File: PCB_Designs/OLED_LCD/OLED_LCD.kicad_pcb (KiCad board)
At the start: 2 copper layers, 110 x 69.5 mm, 27 parts, among them P1 CONN_01X10, P2 CONN_01X16, P3 CONN_01X01, P4 CONN_01X01, P5 CONN_01X01, P6 CONN_01X01, SW1 Rotary_Encoder_Switch, U2 MCP23017, U3 CHERRY-MX

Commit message: Manufacture files added
* Gerbers created
* Drillfiles created
* G-CODE generated (milling information)
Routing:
- net /VCC5: track 404.0 -> 405.6 mm
- net GND: vias 12 -> 13
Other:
- board size 110 x 69.5 mm -> 110 x 60 mm

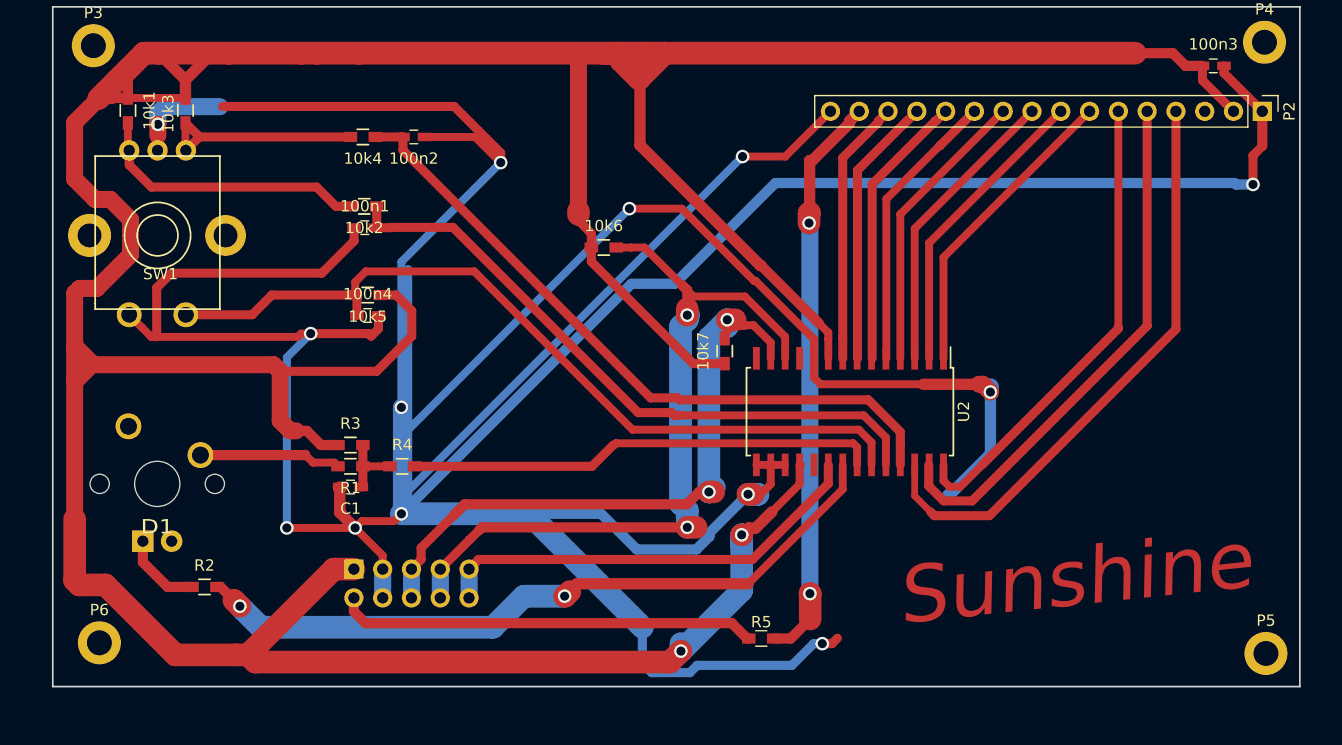
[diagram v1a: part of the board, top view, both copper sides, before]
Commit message: Hotfixes, updates and Photomask
* Edited small error in component placing (OLED_LCD)
* Updated all photomasks in light of recent events
* Generated photomask for OLED_LCD (.pdf)
* Updated all Gerberfiles (.gbr)
* Updated all drillfiles, now merging "plated" and unplated TH (.drl)
* With merge; all Non Plated Through Hole drills deleted (-NPTH.drl)
* Generated new G-CODE for all PCB (.ngc, .svg)
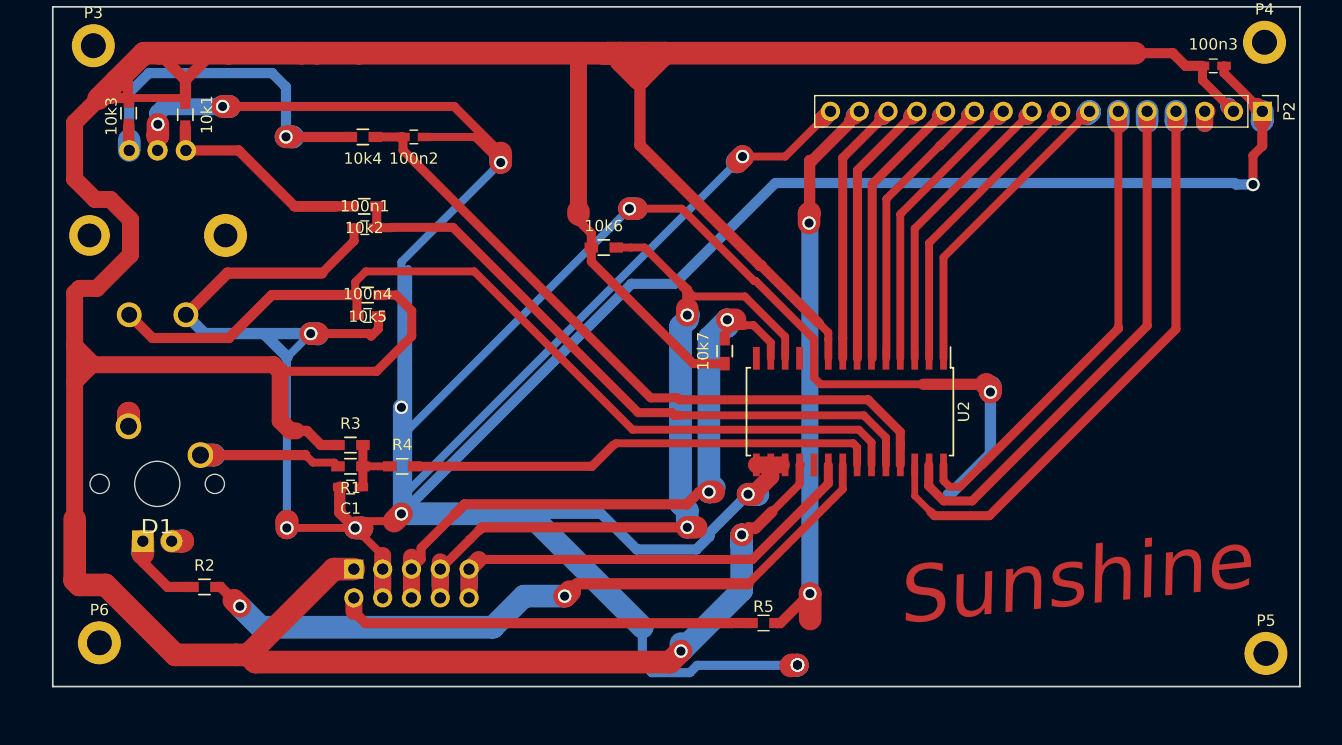
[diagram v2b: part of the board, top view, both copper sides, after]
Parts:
- SW1: moved to B.Cu
- moved 10k1 5.08 mm to (90.1, 87.8)
- moved 10k3 5.02 mm to (85.1, 87.7)
- moved R5 1.38 mm to (141.1, 132.7)
- turned SW1 to 0 degrees
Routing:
- net Net-(10k3-Pad1): track 19.2 -> 34.4 mm, vias 0 -> 1
- net /ENCODERSW: track 72.9 -> 82.0 mm
- net GND: track 519.4 -> 527.8 mm, vias 13 -> 15
- net /SDA#: track 58.5 -> 61.2 mm
- net Net-(10k1-Pad2): track 24.9 -> 22.4 mm
- net Net-(P2-Pad3): track 0.36 -> 2.71 mm
- net Net-(R1-Pad2): track 12.6 -> 14.9 mm
- net /SCL#: track 69.5 -> 71.7 mm
- net Net-(D1-Pad2): track 7.10 -> 9.21 mm
- net /INTA: track 39.1 -> 40.7 mm
- net /LCD_BACKLIGHT: track 50.7 -> 52.1 mm
- net /E: track 42.0 -> 43.3 mm
- net /D7: track 23.5 -> 24.7 mm
- net /D6: track 24.0 -> 25.2 mm
- net /D5: track 24.5 -> 25.7 mm
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
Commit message: New stuff
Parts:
- moved 100n2 5.25 mm to (106.0, 92.9), turned to 0 degrees
- moved 10k3 4.99 mm to (90.1, 87.7)
- moved 10k1 4.98 mm to (85.1, 87.6)
- moved 10k4 1.23 mm to (106.0, 91.0)
- moved 10k2 1.08 mm to (106.0, 94.9)
- moved 100n1 1.08 mm to (106.1, 96.7)
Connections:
- SW1 pad 1: Net-(10k3-Pad1) -> Net-(10k1-Pad2)
- SW1 pad 3: Net-(10k1-Pad2) -> Net-(10k3-Pad1)
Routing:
- net Net-(10k3-Pad1): track 34.4 -> 26.0 mm, vias 1 -> 0
- net GND: track 527.8 -> 521.3 mm
- net Net-(10k1-Pad2): track 22.4 -> 24.5 mm
- net /ENCODERB: track 57.2 -> 57.7 mm

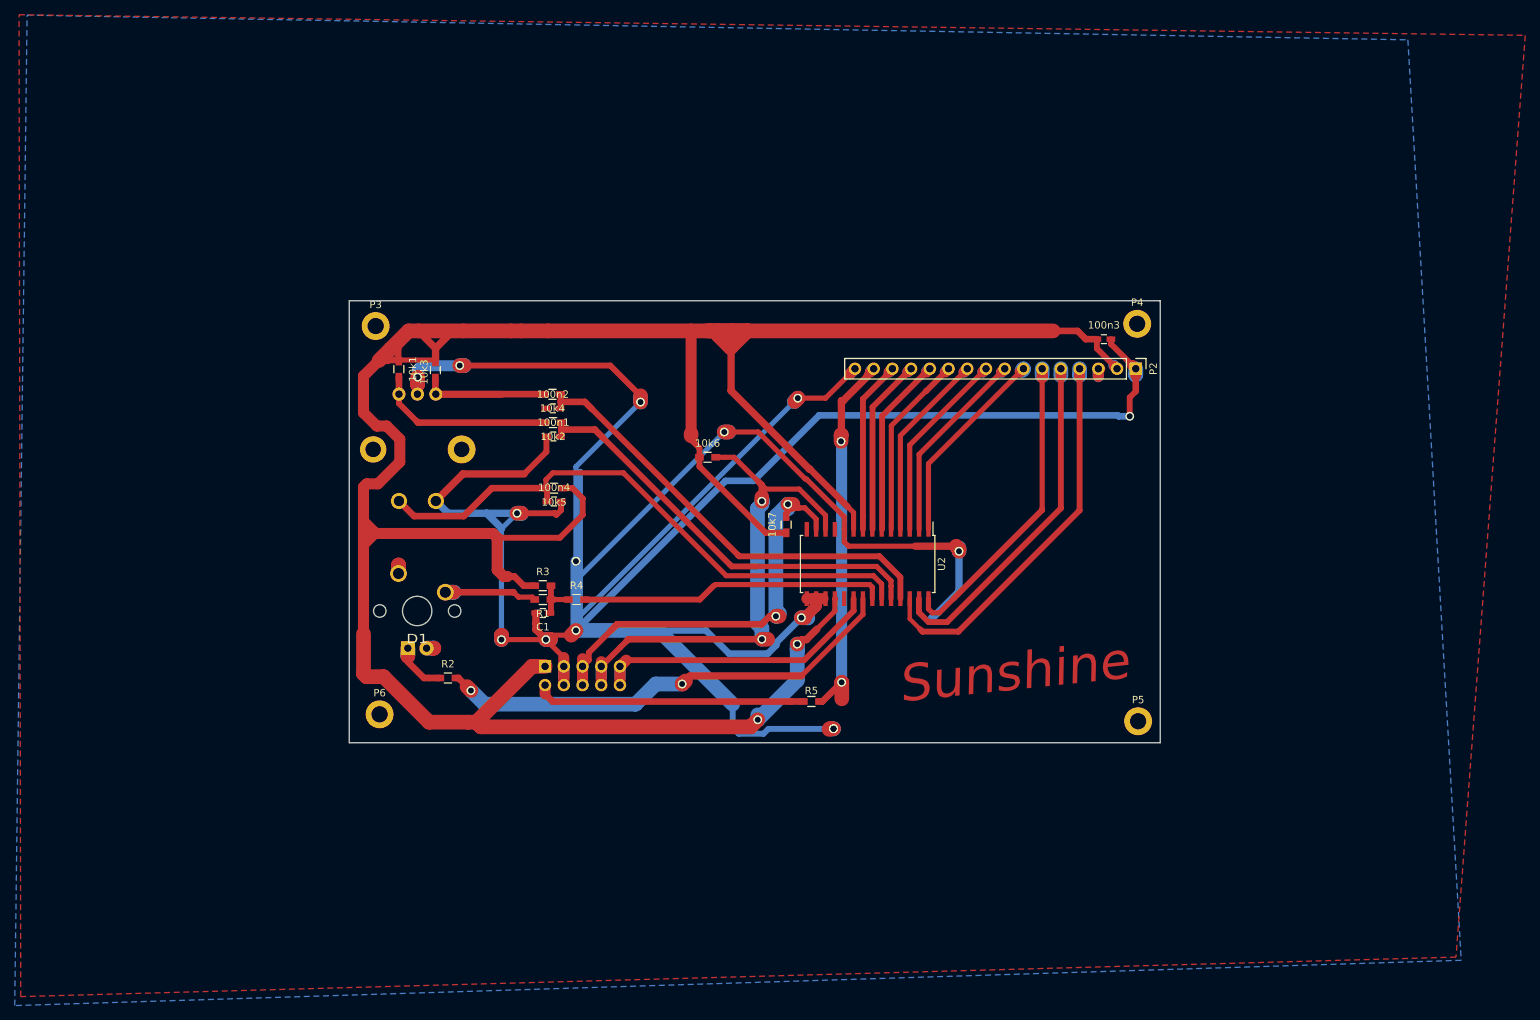
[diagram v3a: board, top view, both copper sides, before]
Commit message: OLED new layout
* Added few components to OLED_LCD pcb.
* Extended PCB layout to make room for all components.
* Generated new LCD photomasks
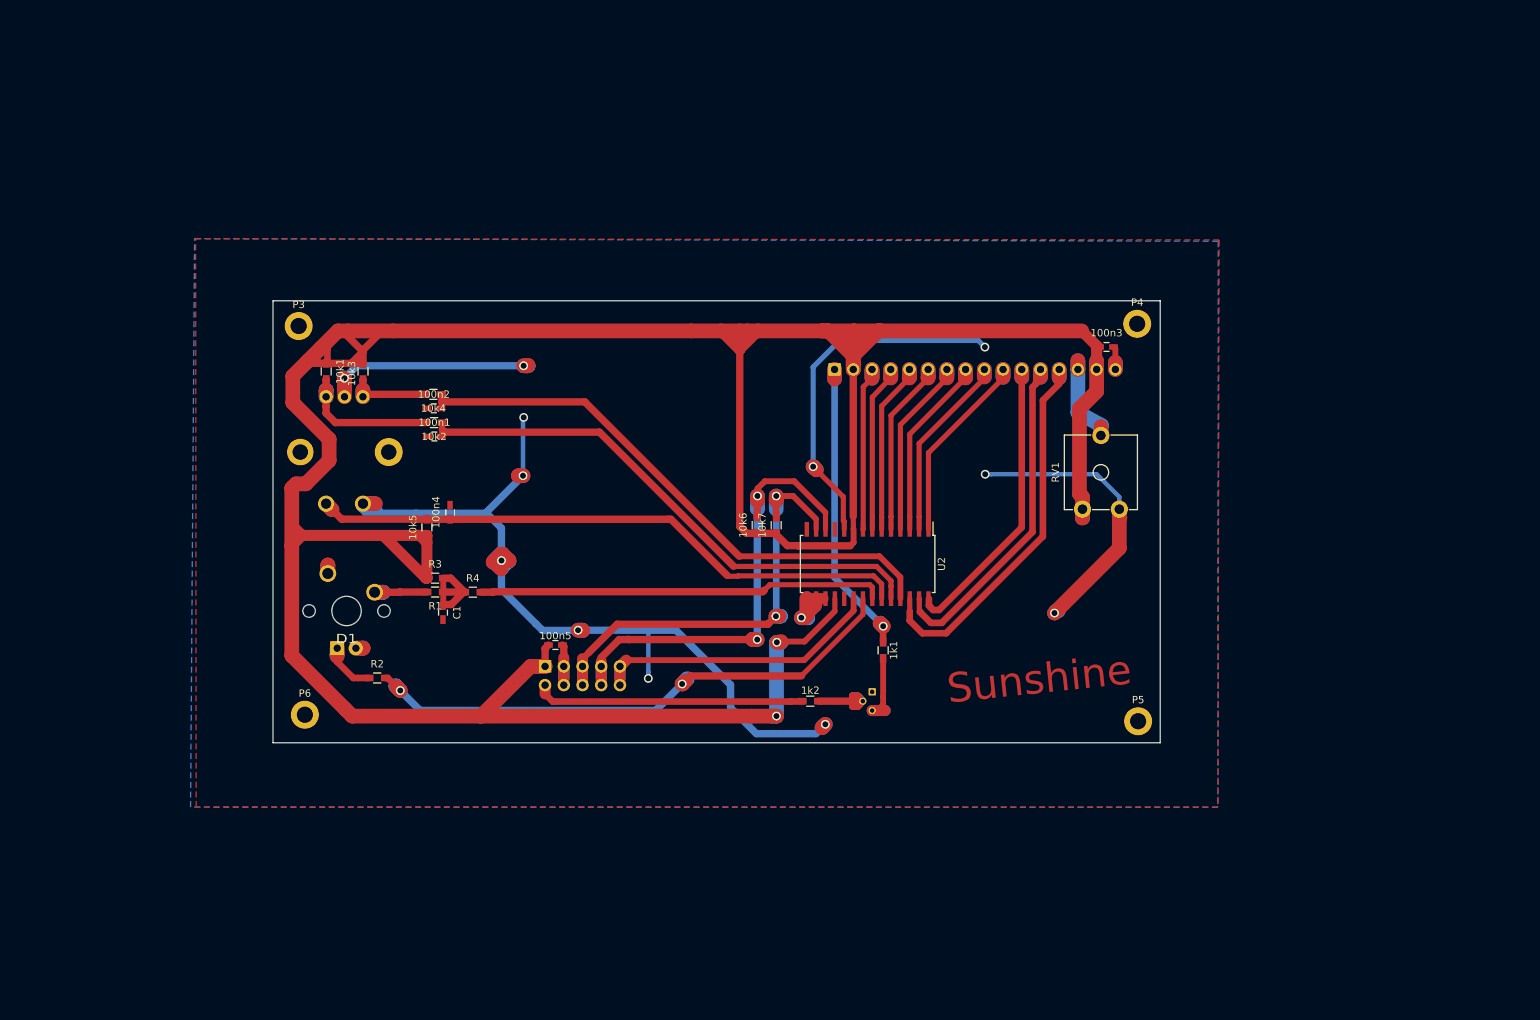
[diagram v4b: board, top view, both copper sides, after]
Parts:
- removed R5: 1k, Resistors_SMD:R_0603_HandSoldering
- added 100n5: 100n, Capacitors_SMD:C_0603_HandSoldering, F.Cu at (106.4, 125.0)
- added 1k1: 1k, Resistors_SMD:R_0603_HandSoldering, F.Cu at (150.8, 125.8)
- added 1k2: 1k, Resistors_SMD:R_0603_HandSoldering, F.Cu at (140.9, 132.7)
- added Q1: PN2222A, TO_SOT_Packages_THT:TO-92_Molded_Narrow, B.Cu at (149.3, 131.4)
- added RV1: POT_TRIM, Potentiometers:Potentiometer_Trimmer_ACP_CA9v_Horizontal_Px10.0mm_Py5.0mm, F.Cu at (182.9, 106.6)
- P2: moved to B.Cu
- moved P2 40.9 mm to (144.2, 87.7)
- moved 10k5 18.1 mm to (88.9, 109.1), turned to 90 degrees
- moved 100n2 16.2 mm to (89.9, 92.9)
- moved 100n1 16.1 mm to (89.9, 96.7)
- moved 10k2 16.1 mm to (89.9, 94.9)
- moved 10k4 16.1 mm to (89.8, 91.0)
- moved R1 14.6 mm to (90.0, 117.9)
- moved R3 14.6 mm to (90.0, 116.0)
- moved 100n4 14.2 mm to (92.1, 107.0), turned to 90 degrees
- moved R4 14.1 mm to (95.2, 117.9)
- moved C1 13.6 mm to (91.1, 120.6), turned to 270 degrees
- moved 10k6 11.4 mm to (133.7, 108.8), turned to 90 degrees
- moved P3 10.4 mm to (71.5, 81.8)
- moved P6 10.1 mm to (72.4, 134.5)
- moved SW1 9.90 mm to (77.7, 98.9)
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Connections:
- P2 pad 1: GND -> /LCD_BACKLIGHT
- P2 pad 10: /D3 -> /D0
- P2 pad 11: /D4 -> /E
- P2 pad 12: /D5 -> /RW
- P2 pad 13: /D6 -> /RS
- P2 pad 14: /D7 -> Net-(P2-Pad14)
- P2 pad 15: /LCD_BACKLIGHT -> /VCC5
- P2 pad 3: Net-(P2-Pad3) -> /D7
- P2 pad 4: /RS -> /D6
- P2 pad 5: /RW -> /D5
- P2 pad 6: /E -> /D4
- P2 pad 7: /D0 -> /D3
- P2 pad 8: /D1 -> /D2
- P2 pad 9: /D2 -> /D1
- P3 pad 1: Net-(P3-Pad1) -> (no net)
- P4 pad 1: Net-(P4-Pad1) -> (no net)
- P5 pad 1: Net-(P5-Pad1) -> (no net)
- P6 pad 1: Net-(P6-Pad1) -> (no net)
- U2 pad 19: Net-(U2-Pad19) -> (no net)
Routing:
- net GND: track 521.3 -> 277.1 mm, vias 15 -> 13
- net /VCC5: track 406.3 -> 463.1 mm
- net /ENCODERB: track 57.7 -> 73.9 mm
- net /ENCODERA: track 60.8 -> 77.0 mm
- net Net-(P2-Pad14): track 0.00 -> 14.5 mm
- net Net-(1k2-Pad2): track 0.00 -> 14.4 mm
- net /BUTTON_2: track 41.6 -> 55.2 mm
- net Net-(10k3-Pad1): track 26.0 -> 13.0 mm
- net /BUTT_LED: track 64.5 -> 76.7 mm
- net Net-(1k1-Pad2): track 0.00 -> 11.6 mm
- net /LCD_BACKLIGHT: track 52.1 -> 43.5 mm, vias 2 -> 1
- net Net-(C1-Pad1): track 6.14 -> 13.8 mm
- net /SDA#: track 61.2 -> 68.4 mm
- net Net-(R1-Pad2): track 14.9 -> 9.42 mm
- net Net-(10k1-Pad2): track 24.5 -> 20.5 mm
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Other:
- board size 110 x 60 mm -> 120.4 x 60 mm

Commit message: Minor changes to OLED
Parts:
- moved 1k1 0.29 mm to (151.0, 126.0)
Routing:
- net GND: track 277.1 -> 265.7 mm
- net /E: track 43.3 -> 38.8 mm
- net /RW: track 47.8 -> 45.3 mm
- net /RS: track 53.1 -> 50.6 mm
- net /VCC5: track 463.1 -> 465.5 mm
- net /BUTT_LED: track 76.7 -> 78.3 mm
- net Net-(1k1-Pad2): track 11.6 -> 12.4 mm
- net Net-(P2-Pad14): track 14.5 -> 15.0 mm

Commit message: ...
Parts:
- moved 100n3 5.55 mm to (181.0, 90.2)
- moved RV1 2.92 mm to (180.0, 106.3)
- moved 1k1 1.71 mm to (152.6, 126.3)
- moved P3 1.23 mm to (70.4, 82.3)
- moved P6 1.15 mm to (71.2, 134.5)
- moved P5 0.80 mm to (184.7, 135.0)
- moved P4 0.49 mm to (184.8, 81.5)
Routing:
- net Net-(P2-Pad14): track 15.0 -> 19.7 mm
- net /VCC5: track 465.5 -> 467.3 mm
- net /LCD_BACKLIGHT: track 43.9 -> 45.1 mm
- net Net-(1k1-Pad2): track 12.4 -> 11.4 mm
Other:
- board size 120.4 x 60 mm -> 122.1 x 60 mm

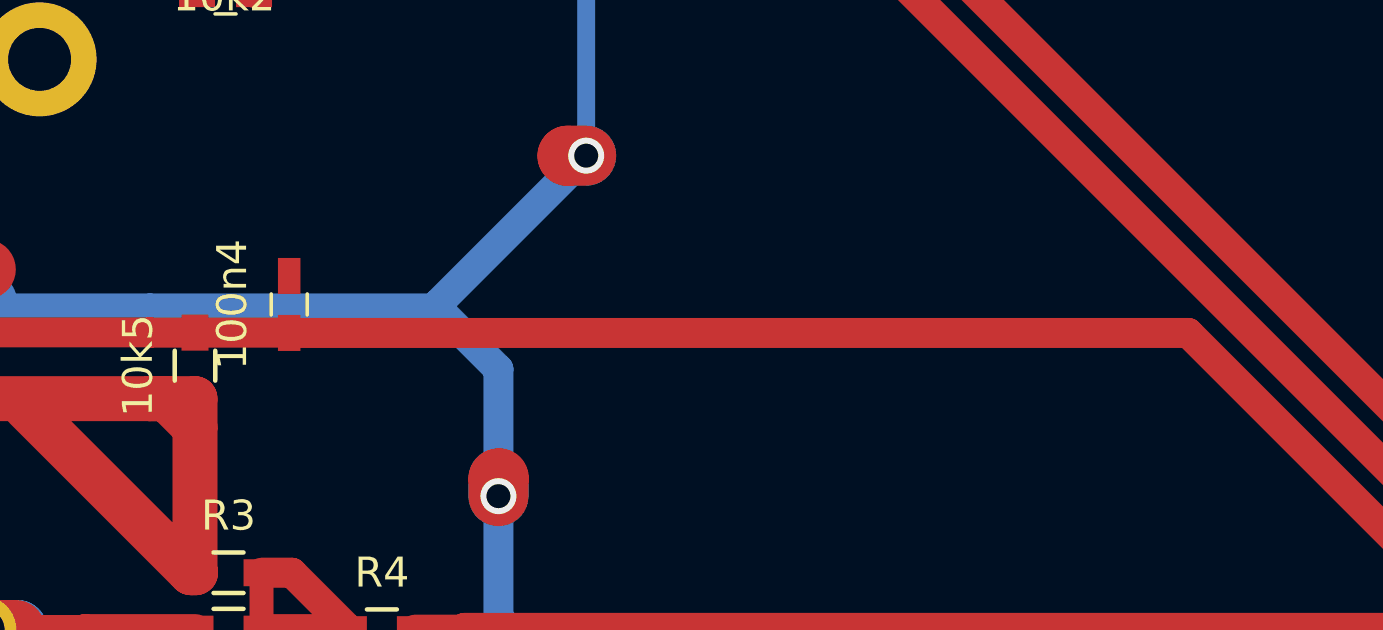
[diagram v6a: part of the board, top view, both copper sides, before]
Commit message: Added missing 10k R on OLED board, diodes on Buttons board
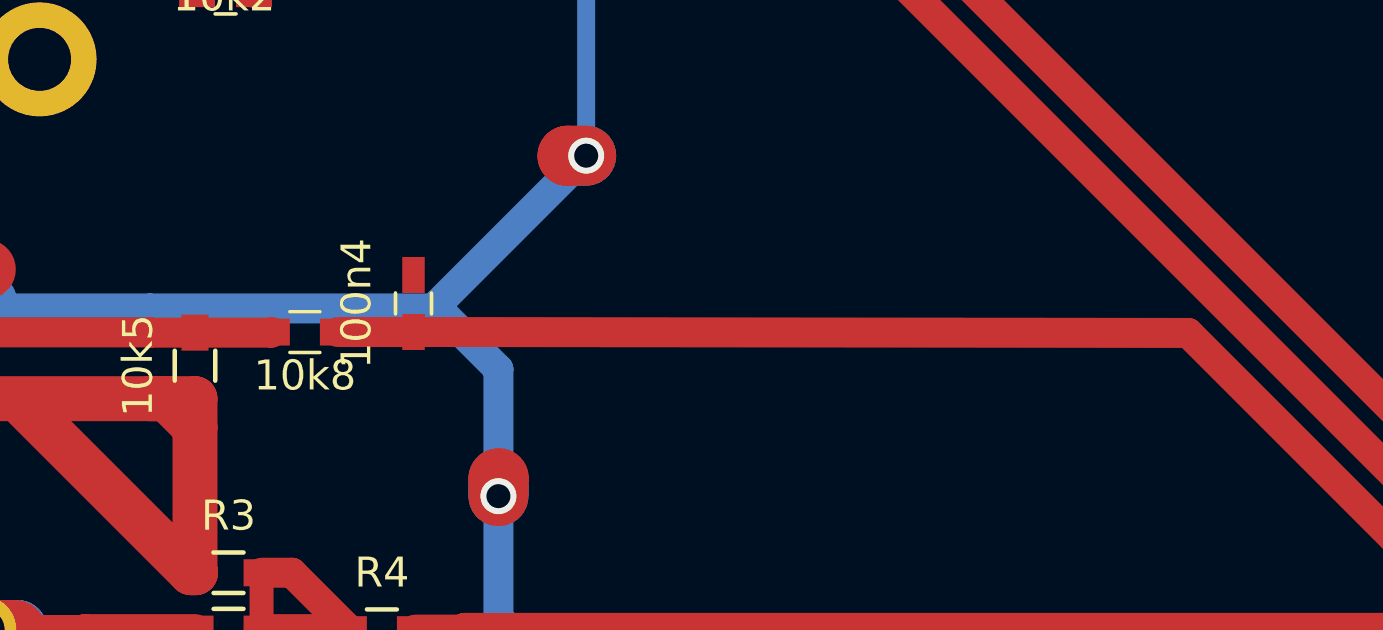
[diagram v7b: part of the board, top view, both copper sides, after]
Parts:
- added 10k8: 10k, Resistors_SMD:R_0603_HandSoldering, F.Cu at (92.6, 108.0)
- moved 100n4 4.14 mm to (96.2, 107.0)
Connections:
- 10k5 pad 2: /ENCODERSW -> Net-(10k5-Pad2)
- P3 pad 1: (no net) -> Net-(P3-Pad1)
- P4 pad 1: (no net) -> Net-(P4-Pad1)
- P5 pad 1: (no net) -> Net-(P5-Pad1)
- P6 pad 1: (no net) -> Net-(P6-Pad1)
- SW1 pad 4: /ENCODERSW -> Net-(10k5-Pad2)
- U2 pad 19: (no net) -> Net-(U2-Pad19)
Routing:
- net /ENCODERSW: track 84.2 -> 62.6 mm
- net Net-(10k5-Pad2): track 0.00 -> 19.4 mm
